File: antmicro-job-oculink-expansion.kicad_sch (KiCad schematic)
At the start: 22 parts, among them J1 OCuLink_x4_Amphenol_G14A42121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, J2 Plug_Samtec_ERM8_2x40_ERM8-04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, U1 MAX3373EEKA+

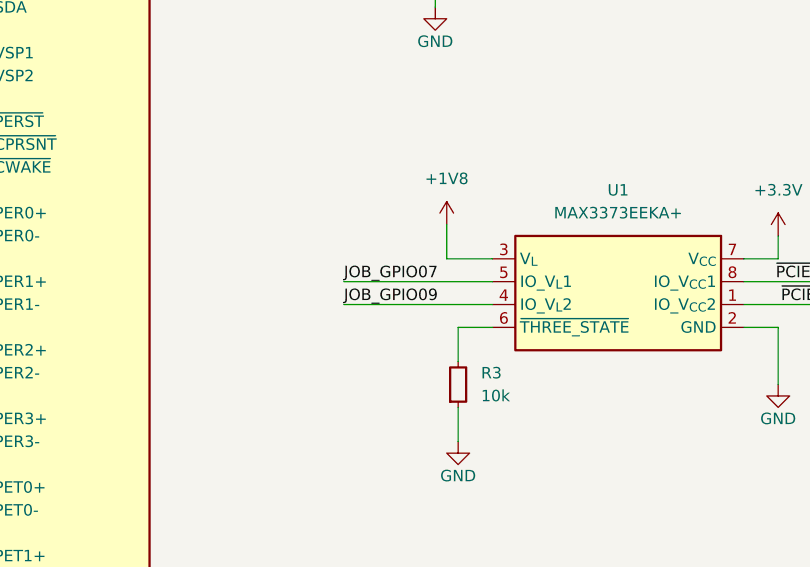
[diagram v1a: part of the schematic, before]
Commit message: [#74340] Routing fixes
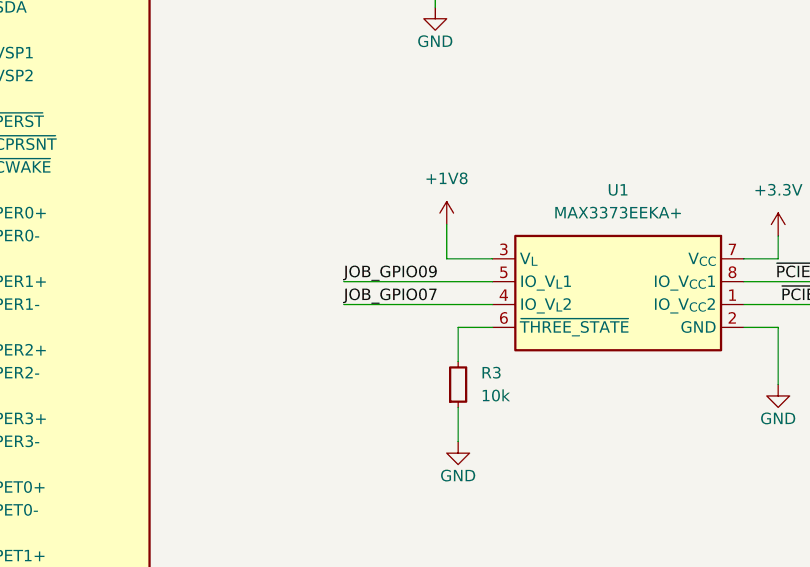
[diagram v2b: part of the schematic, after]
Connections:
- net JOB_GPIO07: now also U1.4 (IO_V_{L}2); no longer U1.5 (IO_V_{L}1)
- net JOB_GPIO09: now also U1.5 (IO_V_{L}1); no longer U1.4 (IO_V_{L}2)
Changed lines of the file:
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@@
 	(wire
 		(pts
-			(xy 185.42 81.28) (xy 201.93 81.28)
-		)
-		(stroke
-			(width 0)
-			(type default)
-		)
-	)
-	(wire
-		(pts
 			(xy 67.31 49.53) (xy 67.31 41.91)
 		)
@@
 	(wire
 		(pts
-			(xy 185.42 78.74) (xy 201.93 78.74)
-		)
-		(stroke
-			(width 0)
-			(type default)
-		)
-	)
-	(wire
-		(pts
 			(xy 55.88 46.99) (xy 69.85 46.99)
 		)
@@
 	(wire
 		(pts
+			(xy 185.42 81.28) (xy 201.93 81.28)
+		)
+		(stroke
+			(width 0)
+			(type default)
+		)
+	)
+	(wire
+		(pts
 			(xy 198.12 87.63) (xy 198.12 83.82)
 		)
@@
 	(wire
 		(pts
+			(xy 185.42 78.74) (xy 201.93 78.74)
+		)
+		(stroke
+			(width 0)
+			(type default)
+		)
+	)
+	(wire
+		(pts
 			(xy 67.31 128.27) (xy 67.31 135.89)
 		)
@@
 		)
 	)
-	(label "JOB_GPIO07"
-		(at 185.42 78.74 0)
-		(fields_autoplaced yes)
-		(effects
-			(font
-				(size 1.27 1.27)
-			)
-			(justify left bottom)
-		)
-	)
-	(label "JOB_GPIO09"
-		(at 185.42 81.28 0)
+	(label "PCIE_RX0-"
+		(at 128.27 73.66 0)
 		(fields_autoplaced yes)
 		(effects
@@
 		)
 	)
-	(label "PCIE_RX0-"
-		(at 128.27 73.66 0)
+	(label "PCIE_TX0-"
+		(at 55.88 44.45 0)
 		(fields_autoplaced yes)
 		(effects
@@
 		)
 	)
-	(label "PCIE_TX0-"
-		(at 55.88 44.45 0)
+	(label "PCIE_TX0+"
+		(at 128.27 101.6 0)
 		(fields_autoplaced yes)
 		(effects
@@
 		)
 	)
-	(label "PCIE_TX0+"
-		(at 128.27 101.6 0)
+	(label "JOB_GPIO07"
+		(at 185.42 81.28 0)
 		(fields_autoplaced yes)
 		(effects
@@
 		)
 	)
+	(label "JOB_GPIO09"
+		(at 185.42 78.74 0)
+		(fields_autoplaced yes)
+		(effects
+			(font
+				(size 1.27 1.27)
+			)
+			(justify left bottom)
+		)
+	)

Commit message: [#74340] Finished applying fixes
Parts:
- removed TP3, TP4: TP_1.5mm_SMD, antmicro-footprints:TP_SMD_1.5mm, symbol antmicroTestPoints:TP_1.5mm_SMD
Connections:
- net ~{PCIE_CPRSNT}: now also U1.1 (IO_V_{CC}2); no longer U1.8 (IO_V_{CC}1)
- net ~{PCIE_CWAKE}: now also U1.8 (IO_V_{CC}1); no longer U1.1 (IO_V_{CC}2)
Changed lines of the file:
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@@
 	(title_block
 		(title "Jetson Orin Baseboard OCuLink Expansion")
-		(date "2025-03-14")
+		(date "2025-03-18")
 		(rev "1.0.0")
 		(company "Antmicro Ltd")
@@
 	(wire
 		(pts
-			(xy 245.11 78.74) (xy 229.87 78.74)
+			(xy 64.77 133.35) (xy 69.85 133.35)
 		)
 		(stroke
@@
 	(wire
 		(pts
-			(xy 64.77 133.35) (xy 69.85 133.35)
+			(xy 195.58 45.72) (xy 185.42 45.72)
 		)
 		(stroke
@@
 	(wire
 		(pts
-			(xy 195.58 45.72) (xy 185.42 45.72)
+			(xy 128.27 55.88) (xy 142.24 55.88)
 		)
 		(stroke
@@
 	(wire
 		(pts
-			(xy 128.27 55.88) (xy 142.24 55.88)
+			(xy 69.85 118.11) (xy 64.77 118.11)
 		)
 		(stroke
@@
 	(wire
 		(pts
-			(xy 69.85 118.11) (xy 64.77 118.11)
+			(xy 195.58 35.56) (xy 195.58 38.1)
 		)
 		(stroke
@@
 	(wire
 		(pts
-			(xy 195.58 35.56) (xy 195.58 38.1)
+			(xy 58.42 115.57) (xy 69.85 115.57)
 		)
 		(stroke
@@
 	(wire
 		(pts
-			(xy 58.42 115.57) (xy 69.85 115.57)
+			(xy 67.31 57.15) (xy 67.31 64.77)
 		)
 		(stroke
@@
 	(wire
 		(pts
-			(xy 67.31 57.15) (xy 67.31 64.77)
+			(xy 245.11 81.28) (xy 229.87 81.28)
 		)
 		(stroke
@@
 	(wire
 		(pts
-			(xy 245.11 81.28) (xy 229.87 81.28)
-		)
-		(stroke
-			(width 0)
-			(type default)
-		)
-	)
-	(wire
-		(pts
 			(xy 185.42 35.56) (xy 185.42 38.1)
 		)
@@
 	(wire
 		(pts
+			(xy 245.11 78.74) (xy 229.87 78.74)
+		)
+		(stroke
+			(width 0)
+			(type default)
+		)
+	)
+	(wire
+		(pts
 			(xy 106.68 63.5) (xy 121.92 63.5)
 		)
@@
 		)
 	)
+	(label "~{PCIE_CWAKE}"
+		(at 245.11 78.74 180)
+		(fields_autoplaced yes)
+		(effects
+			(font
+				(size 1.27 1.27)
+			)
+			(justify right bottom)
+		)
+	)
 	(label "PCIE_RX0+"
 		(at 95.25 49.53 180)
@@
 		)
 	)
+	(label "~{PCIE_CPRSNT}"
+		(at 245.11 81.28 180)
+		(fields_autoplaced yes)
+		(effects
+			(font
+				(size 1.27 1.27)
+			)
+			(justify right bottom)
+		)
+	)
 	(label "JOB_GPIO07"
 		(at 185.42 81.28 0)
@@
 		)
 	)
-	(label "~{PCIE_CWAKE}"
-		(at 245.11 81.28 180)
-		(fields_autoplaced yes)
-		(effects
-			(font
-				(size 1.27 1.27)
-			)
-			(justify right bottom)
-		)
-	)
 	(label "JOB_GPIO09"
 		(at 185.42 78.74 0)
@@
 		)
 	)
-	(label "~{PCIE_CPRSNT}"
-		(at 245.11 78.74 180)
-		(fields_autoplaced yes)
-		(effects
-			(font
-				(size 1.27 1.27)
-			)
-			(justify right bottom)
-		)
-	)
 	(label "I2C_SCL"
 		(at 128.27 45.72 0)
@@
 	)
 	(symbol
-		(lib_id "antmicroTestPoints:TP_1.5mm_SMD")
-		(at 106.68 66.04 180)
-		(unit 1)
-		(exclude_from_sim no)
-		(in_bom no)
-		(on_board yes)
-		(dnp no)
-		(property "Reference" "TP4"
-			(at 99.06 66.294 0)
-			(effects
-				(font
-					(size 1.27 1.27)
-					(thickness 0.15)
-				)
-				(justify right)
-			)
-		)
-		(property "Value" "TP_1.5mm_SMD"
-			(at 91.44 58.42 0)
-			(effects
-				(font
-					(size 1.27 1.27)
-					(thickness 0.15)
-				)
-				(justify left bottom)
-				(hide yes)
-			)
-		)
-		(property "Footprint" "antmicro-footprints:TP_SMD_1.5mm"
-			(at 91.44 55.88 0)
-			(effects
-				(font
-					(size 1.27 1.27)
-					(thickness 0.15)
-				)
-				(justify left bottom)
-				(hide yes)
-			)
-		)
-		(property "Datasheet" ""
-			(at 88.9 53.34 0)
-			(effects
-				(font
-					(size 1.27 1.27)
-					(thickness 0.15)
-				)
-				(justify left bottom)
-				(hide yes)
-			)
-		)
-		(property "Description" "test point, SMT"
-			(at 106.68 66.04 0)
-			(effects
-				(font
-					(size 1.27 1.27)
-				)
-				(hide yes)
-			)
-		)
-		(property "MPN" ""
-			(at 106.68 66.04 0)
-			(effects
-				(font
-					(size 1.27 1.27)
-				)
-				(hide yes)
-			)
-		)
-		(property "Manufacturer" ""
-			(at 106.68 66.04 0)
-			(effects
-				(font
-					(size 1.27 1.27)
-				)
-				(hide yes)
-			)
-		)
-		(property "Author" "Antmicro"
-			(at 91.44 50.8 0)
-			(effects
-				(font
-					(size 1.27 1.27)
-					(thickness 0.15)
-				)
-				(justify left bottom)
-				(hide yes)
-			)
-		)
-		(property "License" "Apache-2.0"
-			(at 91.44 48.26 0)
-			(effects
-				(font
-					(size 1.27 1.27)
-					(thickness 0.15)
-				)
-				(justify left bottom)
-				(hide yes)
-			)
-		)
-		(pin "1"
-		)
-		(instances
-			(project "antmicro-job-oculink-expansion"
-				(path "/195f80bc-f1ce-461e-9433-be011ba7464b"
-					(reference "TP4")
-					(unit 1)
-				)
-			)
-		)
-	)
-	(symbol
 		(lib_id "antmicroResistors0402:R_10k_0402")
 		(at 198.12 92.71 90)
@@
 					(unit 1)
 				)
-			)
-		)
-	)
-	(symbol
-		(lib_id "antmicroTestPoints:TP_1.5mm_SMD")
-		(at 106.68 63.5 180)
-		(unit 1)
-		(exclude_from_sim no)
-		(in_bom no)
-		(on_board yes)
-		(dnp no)
-		(property "Reference" "TP3"
-			(at 100.838 63.5 0)
-			(effects
-				(font
-					(size 1.27 1.27)
-					(thickness 0.15)
-				)
-			)
-		)
-		(property "Value" "TP_1.5mm_SMD"
-			(at 91.44 55.88 0)
-			(effects
-				(font
-					(size 1.27 1.27)
-					(thickness 0.15)
-				)
-				(justify left bottom)
-				(hide yes)
-			)
-		)
-		(property "Footprint" "antmicro-footprints:TP_SMD_1.5mm"
-			(at 91.44 53.34 0)
-			(effects
-				(font
-					(size 1.27 1.27)
-					(thickness 0.15)
-				)
-				(justify left bottom)
-				(hide yes)
-			)
-		)
-		(property "Datasheet" ""
-			(at 88.9 50.8 0)
-			(effects
-				(font
-					(size 1.27 1.27)
-					(thickness 0.15)
-				)
-				(justify left bottom)
-				(hide yes)
-			)
-		)
-		(property "Description" "test point, SMT"
-			(at 106.68 63.5 0)
-			(effects
-				(font
-					(size 1.27 1.27)
-				)
-				(hide yes)
-			)
-		)
-		(property "MPN" ""
-			(at 106.68 63.5 0)
-			(effects
-				(font
-					(size 1.27 1.27)
-				)
-				(hide yes)
-			)
-		)
-		(property "Manufacturer" ""
-			(at 106.68 63.5 0)
-			(effects
-				(font
-					(size 1.27 1.27)
-				)
-				(hide yes)
-			)
-		)
-		(property "Author" "Antmicro"
-			(at 91.44 48.26 0)
-			(effects
-				(font
-					(size 1.27 1.27)
-					(thickness 0.15)
-				)
-				(justify left bottom)
-				(hide yes)
-			)
-		)
-		(property "License" "Apache-2.0"
-			(at 91.44 45.72 0)
-			(effects
-				(font
-					(size 1.27 1.27)
-					(thickness 0.15)
-				)
-				(justify left bottom)
-				(hide yes)
-			)
-		)
-		(pin "1"
-		)
-		(instances
-			(project "antmicro-job-oculink-expansion"
-				(path "/195f80bc-f1ce-461e-9433-be011ba7464b"
-					(reference "TP3")
-					(unit 1)
-				)

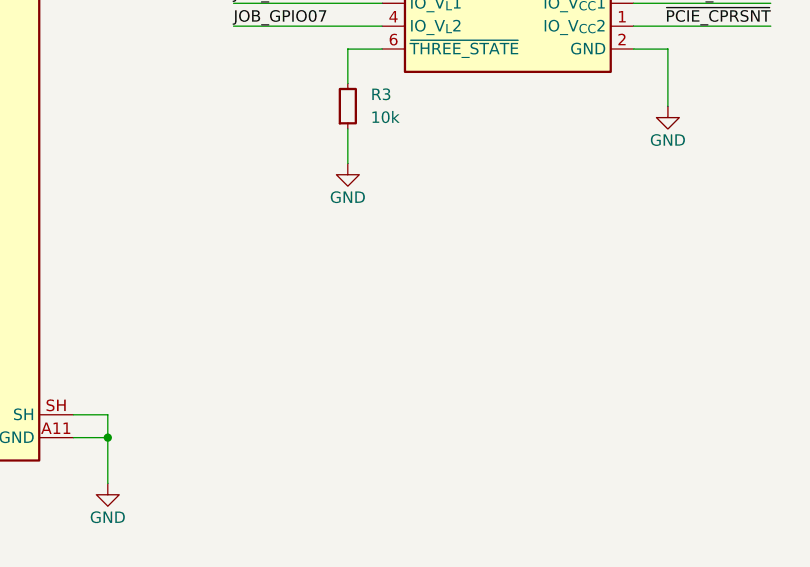
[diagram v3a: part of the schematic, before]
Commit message: [#74340] Add mounting hole
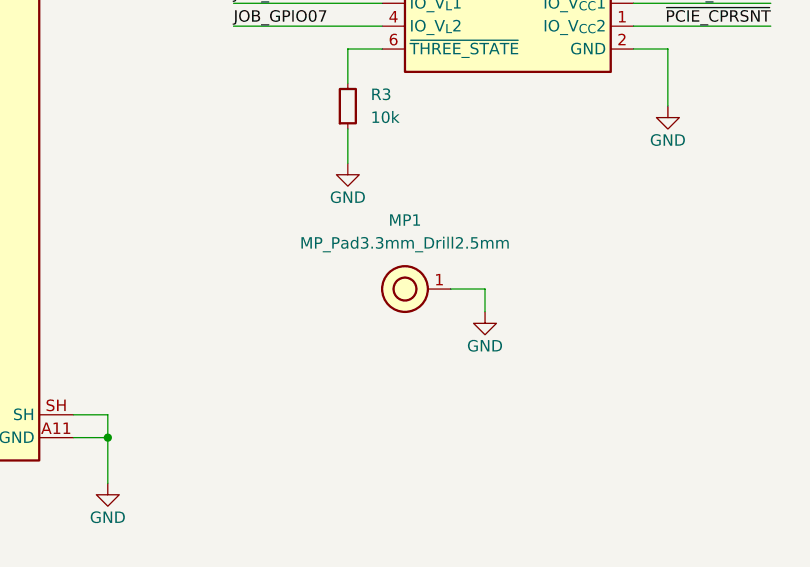
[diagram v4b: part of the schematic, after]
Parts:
- added MP1: MP_Pad3.3mm_Drill2.5mm, antmicro-footprints:MP_Pad3.3mm_Drill2.5mm, symbol antmicroMechanicalParts:MP_Pad3.3mm_Drill2.5mm
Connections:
- net GND: now also MP1.1
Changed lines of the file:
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@@
 	(wire
 		(pts
+			(xy 213.36 110.49) (xy 209.55 110.49)
+		)
+		(stroke
+			(width 0)
+			(type default)
+		)
+	)
+	(wire
+		(pts
 			(xy 55.88 46.99) (xy 69.85 46.99)
 		)
@@
 	(wire
 		(pts
+			(xy 213.36 113.03) (xy 213.36 110.49)
+		)
+		(stroke
+			(width 0)
+			(type default)
+		)
+	)
+	(wire
+		(pts
 			(xy 176.53 38.1) (xy 176.53 35.56)
 		)
@@
 	)
 	(symbol
+		(lib_id "antmicropower:GND")
+		(at 213.36 113.03 0)
+		(mirror y)
+		(unit 1)
+		(exclude_from_sim no)
+		(in_bom yes)
+		(on_board yes)
+		(dnp no)
+		(fields_autoplaced yes)
+		(property "Reference" "#PWR020"
+			(at 213.36 119.38 0)
+			(effects
+				(font
+					(size 1.27 1.27)
+				)
+				(justify left bottom)
+				(hide yes)
+			)
+		)
+		(property "Value" "GND"
+			(at 213.36 116.84 0)
+			(effects
+				(font
+					(size 1.27 1.27)
+					(thickness 0.15)
+				)
+			)
+		)
+		(property "Footprint" ""
+			(at 204.47 120.65 0)
+			(effects
+				(font
+					(size 1.27 1.27)
+					(thickness 0.15)
+				)
+				(justify left bottom)
+				(hide yes)
+			)
+		)
+		(property "Datasheet" ""
+			(at 204.47 125.73 0)
+			(effects
+				(font
+					(size 1.27 1.27)
+					(thickness 0.15)
+				)
+				(justify left bottom)
+				(hide yes)
+			)
+		)
+		(property "Description" ""
+			(at 213.36 113.03 0)
+			(effects
+				(font
+					(size 1.27 1.27)
+				)
+				(hide yes)
+			)
+		)
+		(property "Author" "Antmicro"
+			(at 204.47 120.65 0)
+			(effects
+				(font
+					(size 1.27 1.27)
+					(thickness 0.15)
+				)
+				(justify left bottom)
+				(hide yes)
+			)
+		)
+		(property "License" "Apache-2.0"
+			(at 204.47 123.19 0)
+			(effects
+				(font
+					(size 1.27 1.27)
+					(thickness 0.15)
+				)
+				(justify left bottom)
+				(hide yes)
+			)
+		)
+		(pin "1"
+		)
+		(instances
+			(project "antmicro-job-oculink-expansion"
+				(path "/195f80bc-f1ce-461e-9433-be011ba7464b"
+					(reference "#PWR020")
+					(unit 1)
+				)
+			)
+		)
+	)
+	(symbol
 		(lib_id "antmicropower:+1V8")
 		(at 54.61 124.46 0)
@@
 					(unit 1)
 				)
+			)
+		)
+	)
+	(symbol
+		(lib_id "antmicroMechanicalParts:MP_Pad3.3mm_Drill2.5mm")
+		(at 209.55 110.49 0)
+		(mirror y)
+		(unit 1)
+		(exclude_from_sim no)
+		(in_bom no)
+		(on_board yes)
+		(dnp no)
+		(fields_autoplaced yes)
+		(property "Reference" "MP1"
+			(at 204.47 102.87 0)
+			(effects
+				(font
+					(size 1.27 1.27)
+					(thickness 0.15)
+				)
+			)
+		)
+		(property "Value" "MP_Pad3.3mm_Drill2.5mm"
+			(at 204.47 105.41 0)
+			(effects
+				(font
+					(size 1.27 1.27)
+					(thickness 0.15)
+				)
+			)
+		)
+		(property "Footprint" "antmicro-footprints:MP_Pad3.3mm_Drill2.5mm"
+			(at 196.85 116.84 0)
+			(effects
+				(font
+					(size 1.27 1.27)
+					(thickness 0.15)
+				)
+				(justify left bottom)
+				(hide yes)
+			)
+		)
+		(property "Datasheet" ""
+			(at 192.71 126.06 0)
+			(effects
+				(font
+					(size 1.27 1.27)
+					(thickness 0.15)
+				)
+				(justify left bottom)
+				(hide yes)
+			)
+		)
+		(property "Description" "PCB mounting point template"
+			(at 209.55 110.49 0)
+			(effects
+				(font
+					(size 1.27 1.27)
+				)
+				(hide yes)
+			)
+		)
+		(property "License" "Apache-2.0"
+			(at 196.85 121.92 0)
+			(effects
+				(font
+					(size 1.27 1.27)
+				)
+				(justify left bottom)
+				(hide yes)
+			)
+		)
+		(property "Author" "Antmicro"
+			(at 196.85 124.46 0)
+			(effects
+				(font
+					(size 1.27 1.27)
+				)
+				(justify left bottom)
+				(hide yes)
+			)
+		)
+		(pin "1"
+		)
+		(instances
+			(project ""
+				(path "/195f80bc-f1ce-461e-9433-be011ba7464b"
+					(reference "MP1")
+					(unit 1)
+				)

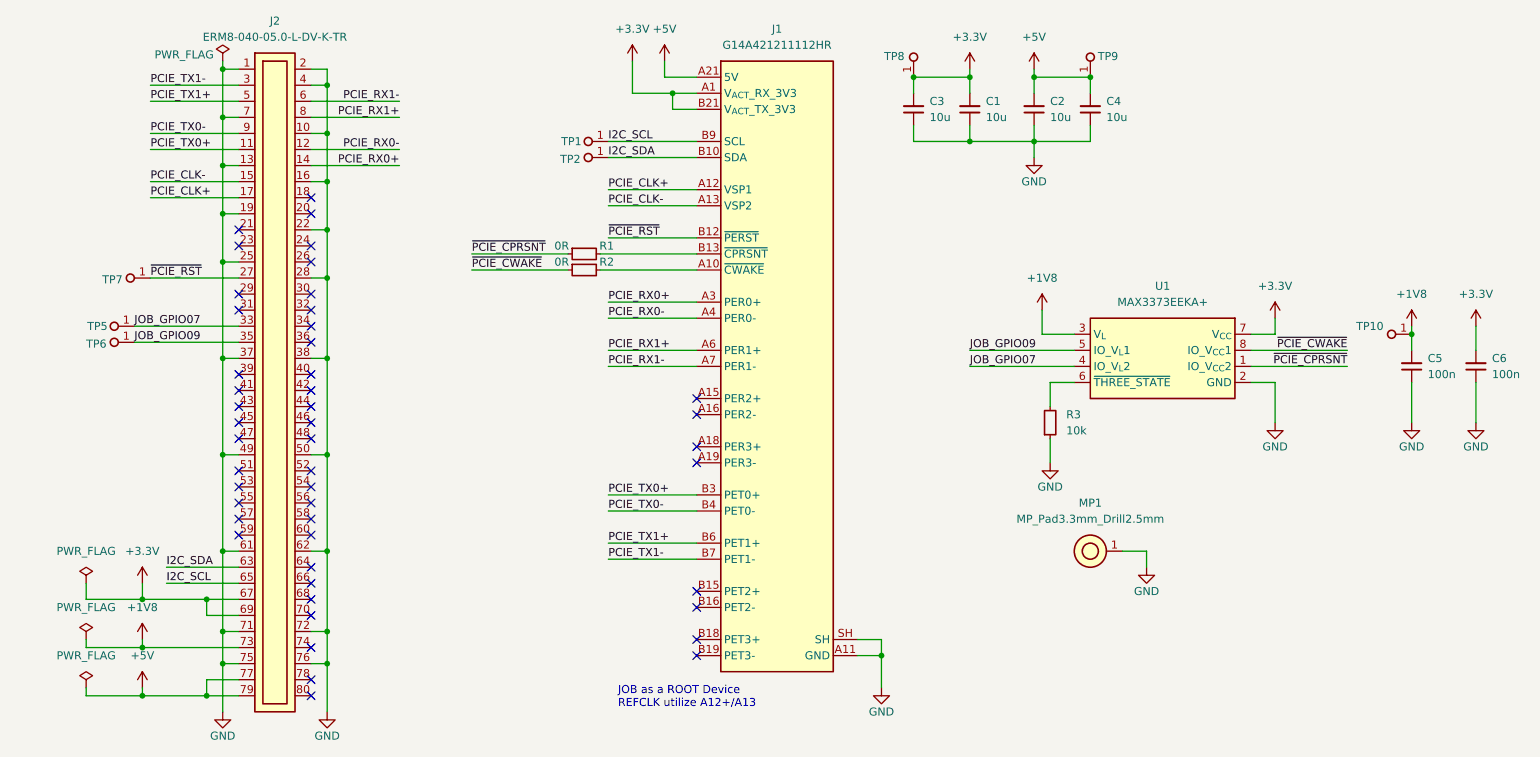
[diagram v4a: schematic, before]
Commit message: [#74340] Minor cosmetic update of schematics
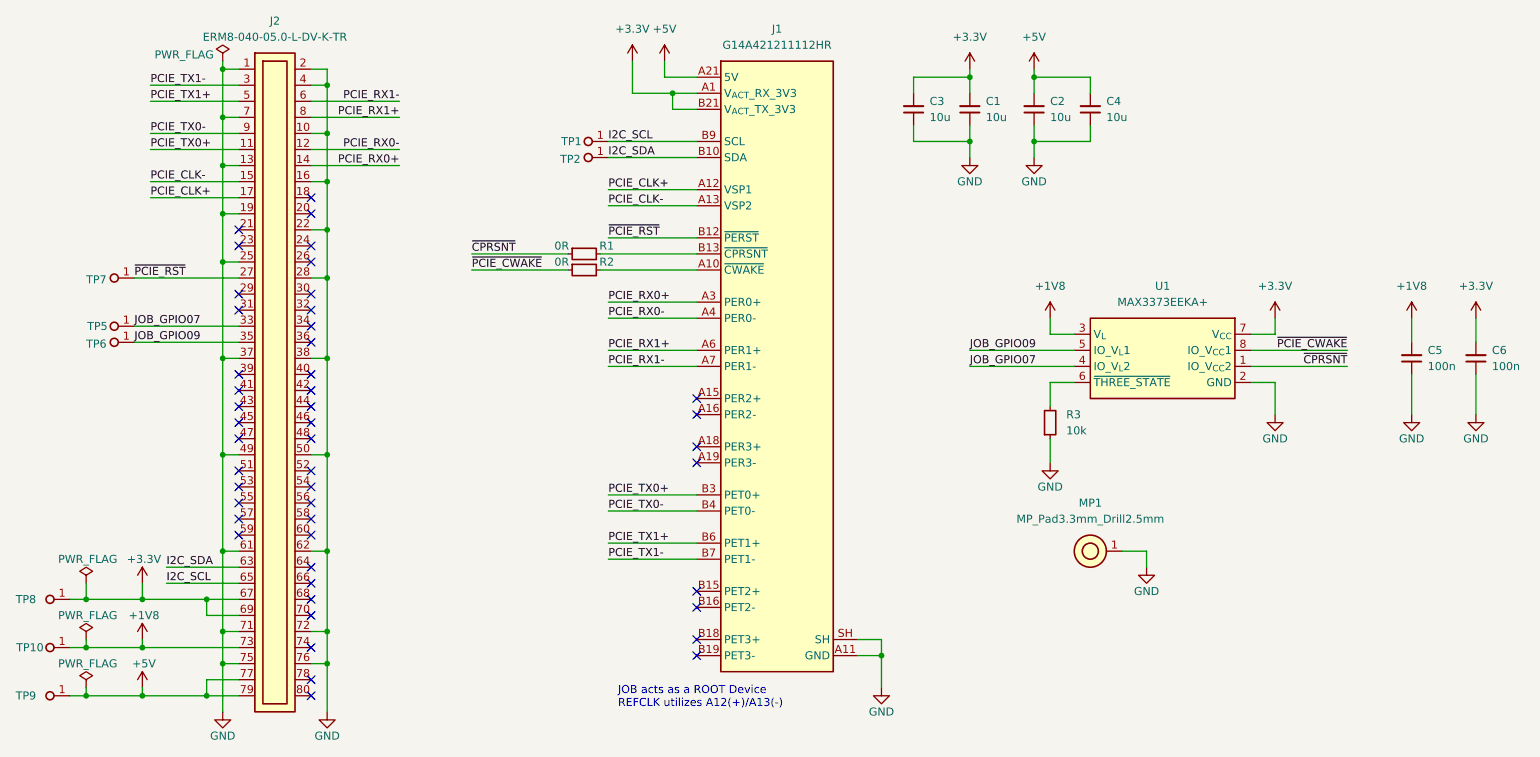
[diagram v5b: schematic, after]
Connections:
- net ~{PCIE_CPRSNT} renamed ~{CPRSNT}
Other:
- note added: "JOB acts as a ROOT Device REFCLK utilizes A12(+)/A13(-)"
- note removed: "JOB as a ROOT Device REFCLK utilize A12+/A13"
- moved on the sheet: C5, C6, TP10, TP7, TP8, TP9
